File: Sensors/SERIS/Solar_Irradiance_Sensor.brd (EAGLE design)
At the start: 100 x 80 mm, 7 parts, among them IC1 LM324N, J1 ARDUINO_R3_SHIELD, U1 V_REG_317DPACK

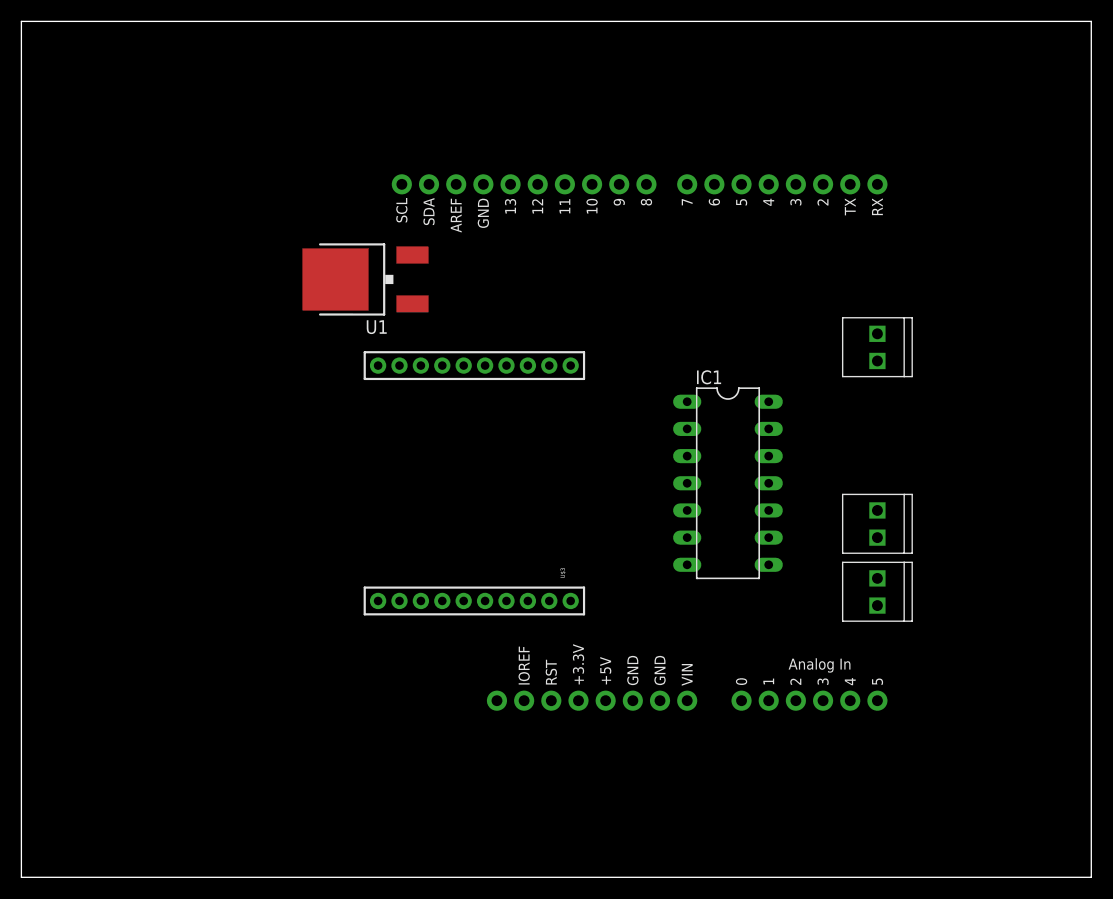
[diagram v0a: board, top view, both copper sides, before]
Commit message: added various files (solar irradiance circuit)
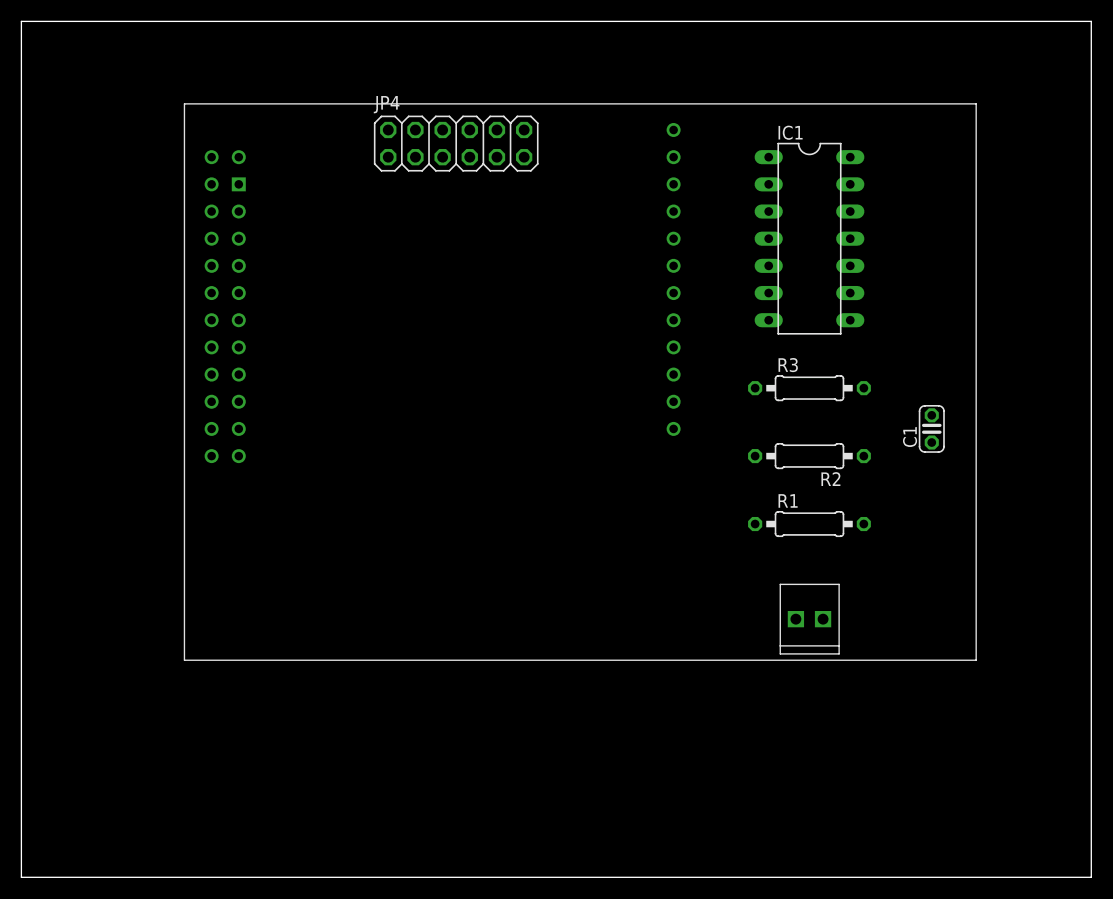
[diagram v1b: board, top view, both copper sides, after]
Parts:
- removed J1: ARDUINO_R3_SHIELD, SparkFun-Boards:UNO_R3_SHIELD
- removed JP2, JP3: M022.54MM_SCREWTERM, SparkFun-Connectors:1X02_2.54_SCREWTERM
- removed U$3: XBEE-1B1, SparkFun-RF:XBEE-1
- removed U1: V_REG_317DPACK, SparkFun-PowerIC:V-REG_DPACK
- added C1: 0.1uF, rcl:C025-024X044
- added JP4: (no value), pinhead:2X06
- added R1, R2: 100k, rcl:0207/10
- added R3: 2k, rcl:0207/10
- added U$1: WASP, wasp:WASP
- moved IC1 24.1 mm to (73.7, 59.7)
- moved JP1 11.4 mm to (74.9, 24.1), turned to 180 degrees
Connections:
- removed net V+: IC1.4
- removed net V-: IC1.11
- removed net VDD: U$3.1
- new net 5V_SENSOR_PWR: IC1.4, JP4.11, JP4.12, U$1.S22
- new net GPIO3: JP4.5
- new net GPIO4: JP4.7
- new net INT: JP4.1
- new net MISO: JP4.6, U$1.A12
- new net MOSI: JP4.4, U$1.A11
- new net N$1: IC1.2, R2.1, R3.2
- new net N$3: C1.1, IC1.3, R1.2
- new net RESET: JP4.3
- new net SCK: JP4.8, U$1.A7
- new net SOLAR_INPUT: JP1.P1, R1.1
- new net SOLAR_OUTPUT: IC1.1, R2.2, U$1.S20
- new net SS: JP4.2, U$1.S12
- net GND: now also C1.2, IC1.11, JP1.P2, JP4.10, JP4.9, R3.1, U$1.A6, U$1.S4; no longer U$3.10
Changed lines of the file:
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@@
 </autorouter>
 <elements>
-<element name="IC1" library="linear" package="DIL14" value="LM324N" x="66.04" y="36.83" rot="R270"/>
-<element name="JP1" library="SparkFun-Connectors" package="1X02_2.54_SCREWTERM" value="M022.54MM_SCREWTERM" x="80.01" y="34.29" rot="R270"/>
-<element name="JP2" library="SparkFun-Connectors" package="1X02_2.54_SCREWTERM" value="M022.54MM_SCREWTERM" x="80.01" y="50.8" rot="R270"/>
-<element name="JP3" library="SparkFun-Connectors" package="1X02_2.54_SCREWTERM" value="M022.54MM_SCREWTERM" x="80.01" y="27.94" rot="R270"/>
-<element name="J1" library="SparkFun-Boards" package="UNO_R3_SHIELD" value="ARDUINO_R3_SHIELD" x="25.4" y="67.31" rot="R270"/>
-<element name="U$3" library="SparkFun-RF" package="XBEE-1" value="XBEE-1B1" x="53.34" y="36.83" rot="R90"/>
-<element name="U1" library="SparkFun-PowerIC" package="V-REG_DPACK" value="V_REG_317DPACK" x="31.75" y="55.88" rot="R90">
-<attribute name="PROD_ID" value="IC-09888" x="31.75" y="55.88" size="1.778" layer="27" rot="R90" display="off"/>
-</element>
+<element name="IC1" library="linear" package="DIL14" value="LM324N" x="73.66" y="59.69" rot="R270"/>
+<element name="JP1" library="SparkFun-Connectors" package="1X02_2.54_SCREWTERM" value="M022.54MM_SCREWTERM" x="74.93" y="24.13" rot="R180"/>
+<element name="U$1" library="wasp" package="WASP" value="WASP" x="50.8" y="54.61"/>
+<element name="R1" library="rcl" package="0207/10" value="100k" x="73.66" y="33.02"/>
+<element name="R2" library="rcl" package="0207/10" value="100k" x="73.66" y="39.37" rot="R180"/>
+<element name="R3" library="rcl" package="0207/10" value="2k" x="73.66" y="45.72"/>
+<element name="C1" library="rcl" package="C025-024X044" value="0.1uF" x="85.09" y="41.91" rot="R90"/>
+<element name="JP4" library="pinhead" package="2X06" value="" x="40.64" y="68.58"/>
 </elements>
 <signals>
-<signal name="V+">
+<signal name="GND">
+<contactref element="IC1" pad="11"/>
+<contactref element="R3" pad="1"/>
+<contactref element="C1" pad="2"/>
+<contactref element="U$1" pad="S4"/>
+<contactref element="U$1" pad="A6"/>
+<contactref element="JP4" pad="9"/>
+<contactref element="JP4" pad="10"/>
+<contactref element="JP1" pad="P2"/>
+<wire x1="85.09" y1="43.18" x2="74.93" y2="24.13" width="0" layer="19" extent="1-1"/>
+<wire x1="77.47" y1="59.69" x2="85.09" y2="43.18" width="0" layer="19" extent="1-1"/>
+<wire x1="60.96" y1="57.15" x2="77.47" y2="59.69" width="0" layer="19" extent="1-1"/>
+<wire x1="44.45" y1="67.31" x2="60.96" y2="57.15" width="0" layer="19" extent="1-1"/>
+<wire x1="44.45" y1="69.85" x2="44.45" y2="67.31" width="0" layer="19" extent="1-1"/>
+<wire x1="68.58" y1="45.72" x2="60.96" y2="57.15" width="0" layer="19" extent="1-1"/>
+<wire x1="20.32" y1="64.77" x2="44.45" y2="67.31" width="0" layer="19" extent="1-1"/>
+</signal>
+<signal name="N$1">
+<contactref element="R3" pad="2"/>
+<contactref element="IC1" pad="2"/>
+<contactref element="R2" pad="1"/>
+<wire x1="78.74" y1="45.72" x2="69.85" y2="64.77" width="0" layer="19" extent="1-1"/>
+<wire x1="78.74" y1="39.37" x2="78.74" y2="45.72" width="0" layer="19" extent="1-1"/>
+</signal>
+<signal name="N$3">
+<contactref element="R1" pad="2"/>
+<contactref element="IC1" pad="3"/>
+<contactref element="C1" pad="1"/>
+<wire x1="78.74" y1="33.02" x2="69.85" y2="62.23" width="0" layer="19" extent="1-1"/>
+<wire x1="85.09" y1="40.64" x2="78.74" y2="33.02" width="0" layer="19" extent="1-1"/>
+</signal>
+<signal name="SOLAR_OUTPUT">
+<contactref element="R2" pad="2"/>
+<contactref element="IC1" pad="1"/>
+<contactref element="U$1" pad="S20"/>
+<wire x1="68.58" y1="39.37" x2="69.85" y2="67.31" width="0" layer="19" extent="1-1"/>
+<wire x1="20.32" y1="44.45" x2="69.85" y2="67.31" width="0" layer="19" extent="1-1"/>
+</signal>
+<signal name="5V_SENSOR_PWR">
+<contactref element="U$1" pad="S22"/>
 <contactref element="IC1" pad="4"/>
+<contactref element="JP4" pad="11"/>
+<contactref element="JP4" pad="12"/>
+<wire x1="46.99" y1="69.85" x2="69.85" y2="59.69" width="0" layer="19" extent="1-1"/>
+<wire x1="46.99" y1="67.31" x2="46.99" y2="69.85" width="0" layer="19" extent="1-1"/>
+<wire x1="20.32" y1="41.91" x2="46.99" y2="69.85" width="0" layer="19" extent="1-1"/>
 </signal>
-<signal name="V-">
-<contactref element="IC1" pad="11"/>
+<signal name="SOLAR_INPUT">
+<contactref element="R1" pad="1"/>
+<contactref element="JP1" pad="P1"/>
+<wire x1="68.58" y1="33.02" x2="72.39" y2="24.13" width="0" layer="19" extent="1-1"/>
 </signal>
-<signal name="VDD">
-<contactref element="U$3" pad="1"/>
+<signal name="INT">
+<contactref element="JP4" pad="1"/>
 </signal>
-<signal name="GND">
-<contactref element="U$3" pad="10"/>
+<signal name="RESET">
+<contactref element="JP4" pad="3"/>
+</signal>
+<signal name="GPIO3">
+<contactref element="JP4" pad="5"/>
+</signal>
+<signal name="GPIO4">
+<contactref element="JP4" pad="7"/>
+</signal>
+<signal name="SCK">
+<contactref element="JP4" pad="8"/>
+<contactref element="U$1" pad="A7"/>
+<wire x1="41.91" y1="69.85" x2="60.96" y2="54.61" width="0" layer="19" extent="1-1"/>
+</signal>
+<signal name="MISO">
+<contactref element="JP4" pad="6"/>
+<contactref element="U$1" pad="A12"/>
+<wire x1="39.37" y1="69.85" x2="60.96" y2="41.91" width="0" layer="19" extent="1-1"/>
+</signal>
+<signal name="MOSI">
+<contactref element="U$1" pad="A11"/>
+<contactref element="JP4" pad="4"/>
+<wire x1="36.83" y1="69.85" x2="60.96" y2="44.45" width="0" layer="19" extent="1-1"/>
+</signal>
+<signal name="SS">
+<contactref element="JP4" pad="2"/>
+<contactref element="U$1" pad="S12"/>
+<wire x1="34.29" y1="69.85" x2="20.32" y2="54.61" width="0" layer="19" extent="1-1"/>
 </signal>
 </signals>

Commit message: eagle circuit update SERIS
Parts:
- JP4: value (none) -> MAX31865
- moved C1 17.3 mm to (80.0, 58.4)
- moved JP1 10.2 mm to (64.8, 25.4), turned to 0 degrees
- moved R2 6.48 mm to (74.9, 45.7), turned to 0 degrees
- moved R3 6.48 mm to (74.9, 39.4)
- moved IC1 2.54 mm to (71.1, 59.7), turned to 90 degrees
- moved JP4 1.80 mm to (39.4, 67.3)
- moved R1 1.27 mm to (74.9, 33.0)
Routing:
- net GND: track 0.00 -> 108.7 mm
- net 5V_SENSOR_PWR: track 0.00 -> 78.1 mm
- net SOLAR_OUTPUT: track 0.00 -> 74.3 mm
- net MISO: track 0.00 -> 36.2 mm
- net MOSI: track 0.00 -> 35.9 mm
- net N$3: track 0.00 -> 30.2 mm
- net SCK: track 0.00 -> 26.1 mm
- net N$1: track 0.00 -> 23.8 mm
- net SS: track 0.00 -> 19.4 mm
- net SOLAR_INPUT: track 0.00 -> 8.66 mm
